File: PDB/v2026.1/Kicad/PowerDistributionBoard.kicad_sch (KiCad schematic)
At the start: 74 parts, among them J1 12V_EXP3, J10 BMS, J11 IMD, J12 Suspension_Linear_Pot1, J13 Suspension_Linear_Pot2, J14 Suspension_Linear_Pot3, J15 Suspension_Linear_Pot4, J16 CCM_Faults, J17 EXP1_5V, J18 RasPI_5V, J19 LATCH_12V, J2 12V_EXP2, J20 Throttle_Sensor, J21 Current_Sensor, J24 Wheel_Sensor1, J25 Wheel_Sensor2, J26 3V3_EXP, J27 BATTERY_12V, J28 BATTERY_GND, J29 BATTERY_24V, J3 12V_EXP1, J31 FAN1_24V, J32 FAN2_24V, J33 PUMP1_24V, J34 PUMP2_24V, J35 24V_EXP1, J4 RTM, J5 CCM_12V, J7 BSPD, J8 LATCH, J9 TSSI, U1 5to3.3_Linear_Regulator, U2 TLV76150DCYR

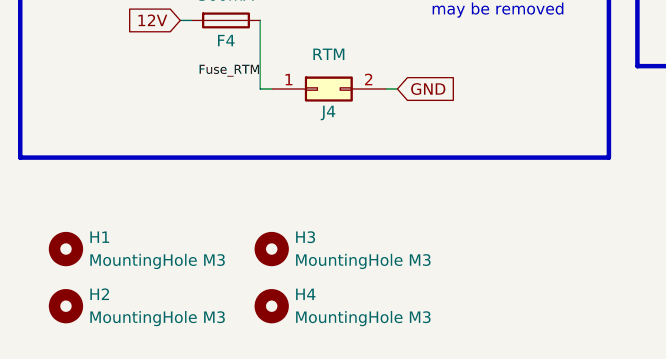
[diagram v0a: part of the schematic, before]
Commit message: Added plated mounting holes, fixed diode
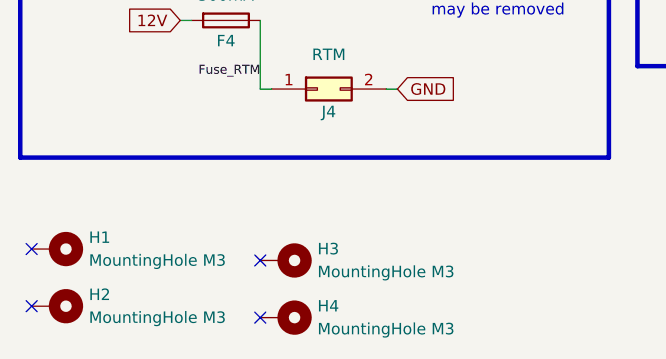
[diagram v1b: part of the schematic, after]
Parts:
- removed H1, H2, H3, H4: MountingHole M3, MountingHole:MountingHole_3.2mm_M3, symbol Mechanical:MountingHole
- added H1, H2, H3, H4: MountingHole M3, MountingHole:MountingHole_3.2mm_M3_Pad, symbol Mechanical:MountingHole_Pad
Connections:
- no-connect marks 12 -> 16

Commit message: Made quick changes: updated fuse footprint
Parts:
- F1, F10, F11, F12, F13, F14, F15, F17, F18, F19, F2, F20, F21, F24, F25, F26, F27, F29, F3, F31, F32, F33, F34, F35, F4, F5, F7, F9, FU1, FU2: footprint 0footprints:649-SERIES-HOLDER -> 0footprints:FUSE_3522-2
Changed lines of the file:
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@@
 			)
 		)
-		(property "Footprint" "0footprints:649-SERIES-HOLDER"
+		(property "Footprint" "0footprints:FUSE_3522-2"
 			(at 223.52 116.332 90)
 			(effects
@@
 			)
 		)
-		(property "Footprint" "0footprints:649-SERIES-HOLDER"
+		(property "Footprint" "0footprints:FUSE_3522-2"
 			(at 38.1 89.662 90)
 			(effects
@@
 			)
 		)
-		(property "Footprint" "0footprints:649-SERIES-HOLDER"
+		(property "Footprint" "0footprints:FUSE_3522-2"
 			(at 168.91 146.812 90)
 			(effects
@@
 			)
 		)
-		(property "Footprint" "0footprints:649-SERIES-HOLDER"
+		(property "Footprint" "0footprints:FUSE_3522-2"
 			(at 168.91 129.032 90)
 			(effects
@@
 			)
 		)
-		(property "Footprint" "0footprints:649-SERIES-HOLDER"
+		(property "Footprint" "0footprints:FUSE_3522-2"
 			(at 222.25 71.882 90)
 			(effects
@@
 			)
 		)
-		(property "Footprint" "0footprints:649-SERIES-HOLDER"
+		(property "Footprint" "0footprints:FUSE_3522-2"
 			(at 38.1 137.922 90)
 			(effects
@@
 			)
 		)
-		(property "Footprint" "0footprints:649-SERIES-HOLDER"
+		(property "Footprint" "0footprints:FUSE_3522-2"
 			(at 100.33 138.938 90)
 			(effects
@@
 			)
 		)
-		(property "Footprint" "0footprints:649-SERIES-HOLDER"
+		(property "Footprint" "0footprints:FUSE_3522-2"
 			(at 38.1 104.902 90)
 			(effects
@@
 			)
 		)
-		(property "Footprint" "0footprints:649-SERIES-HOLDER"
+		(property "Footprint" "0footprints:FUSE_3522-2"
 			(at 154.94 72.898 90)
 			(effects
@@
 			)
 		)
-		(property "Footprint" "0footprints:649-SERIES-HOLDER"
+		(property "Footprint" "0footprints:FUSE_3522-2"
 			(at 223.52 99.822 90)
 			(effects
@@
 			)
 		)
-		(property "Footprint" "0footprints:649-SERIES-HOLDER"
+		(property "Footprint" "0footprints:FUSE_3522-2"
 			(at 154.94 46.228 90)
 			(effects
@@
 			)
 		)
-		(property "Footprint" "0footprints:649-SERIES-HOLDER"
+		(property "Footprint" "0footprints:FUSE_3522-2"
 			(at 168.91 118.872 90)
 			(effects
@@
 			)
 		)
-		(property "Footprint" "0footprints:649-SERIES-HOLDER"
+		(property "Footprint" "0footprints:FUSE_3522-2"
 			(at 27.94 24.892 90)
 			(effects
@@
 			)
 		)
-		(property "Footprint" "0footprints:649-SERIES-HOLDER"
+		(property "Footprint" "0footprints:FUSE_3522-2"
 			(at 223.52 22.098 90)
 			(effects
@@
 			)
 		)
-		(property "Footprint" "0footprints:649-SERIES-HOLDER"
+		(property "Footprint" "0footprints:FUSE_3522-2"
 			(at 168.91 137.922 90)
 			(effects
@@
 			)
 		)
-		(property "Footprint" "0footprints:649-SERIES-HOLDER"
+		(property "Footprint" "0footprints:FUSE_3522-2"
 			(at 38.1 154.432 90)
 			(effects
@@
 			)
 		)
-		(property "Footprint" "0footprints:649-SERIES-HOLDER"
+		(property "Footprint" "0footprints:FUSE_3522-2"
 			(at 96.52 46.228 90)
 			(effects
@@
 			)
 		)
-		(property "Footprint" "0footprints:649-SERIES-HOLDER"
+		(property "Footprint" "0footprints:FUSE_3522-2"
 			(at 222.25 85.852 90)
 			(effects
@@
 			)
 		)
-		(property "Footprint" "0footprints:649-SERIES-HOLDER"
+		(property "Footprint" "0footprints:FUSE_3522-2"
 			(at 120.65 22.098 90)
 			(effects
@@
 			)
 		)
-		(property "Footprint" "0footprints:649-SERIES-HOLDER"
+		(property "Footprint" "0footprints:FUSE_3522-2"
 			(at 38.1 121.412 90)
 			(effects
@@
 			)
 		)
-		(property "Footprint" "0footprints:649-SERIES-HOLDER"
+		(property "Footprint" "0footprints:FUSE_3522-2"
 			(at 96.52 61.468 90)
 			(effects
@@
 			)
 		)
-		(property "Footprint" "0footprints:649-SERIES-HOLDER"
+		(property "Footprint" "0footprints:FUSE_3522-2"
 			(at 100.33 151.638 90)
 			(effects
@@
 			)
 		)
-		(property "Footprint" "0footprints:649-SERIES-HOLDER"
+		(property "Footprint" "0footprints:FUSE_3522-2"
 			(at 168.91 109.982 90)
 			(effects
@@
 			)
 		)
-		(property "Footprint" "0footprints:649-SERIES-HOLDER"
+		(property "Footprint" "0footprints:FUSE_3522-2"
 			(at 100.33 109.728 90)
 			(effects
@@
 			)
 		)
-		(property "Footprint" "0footprints:649-SERIES-HOLDER"
+		(property "Footprint" "0footprints:FUSE_3522-2"
 			(at 260.35 105.918 90)
 			(effects
@@
 			)
 		)
-		(property "Footprint" "0footprints:649-SERIES-HOLDER"
+		(property "Footprint" "0footprints:FUSE_3522-2"
 			(at 261.62 88.138 90)
 			(effects
@@
 			)
 		)
-		(property "Footprint" "0footprints:649-SERIES-HOLDER"
+		(property "Footprint" "0footprints:FUSE_3522-2"
 			(at 100.33 121.412 90)
 			(effects
@@
 			)
 		)
-		(property "Footprint" "0footprints:649-SERIES-HOLDER"
+		(property "Footprint" "0footprints:FUSE_3522-2"
 			(at 27.94 61.468 90)
 			(effects
@@
 			)
 		)
-		(property "Footprint" "0footprints:649-SERIES-HOLDER"
+		(property "Footprint" "0footprints:FUSE_3522-2"
 			(at 154.94 60.198 90)
 			(effects
@@
 			)
 		)
-		(property "Footprint" "0footprints:649-SERIES-HOLDER"
+		(property "Footprint" "0footprints:FUSE_3522-2"
 			(at 154.94 85.598 90)
 			(effects

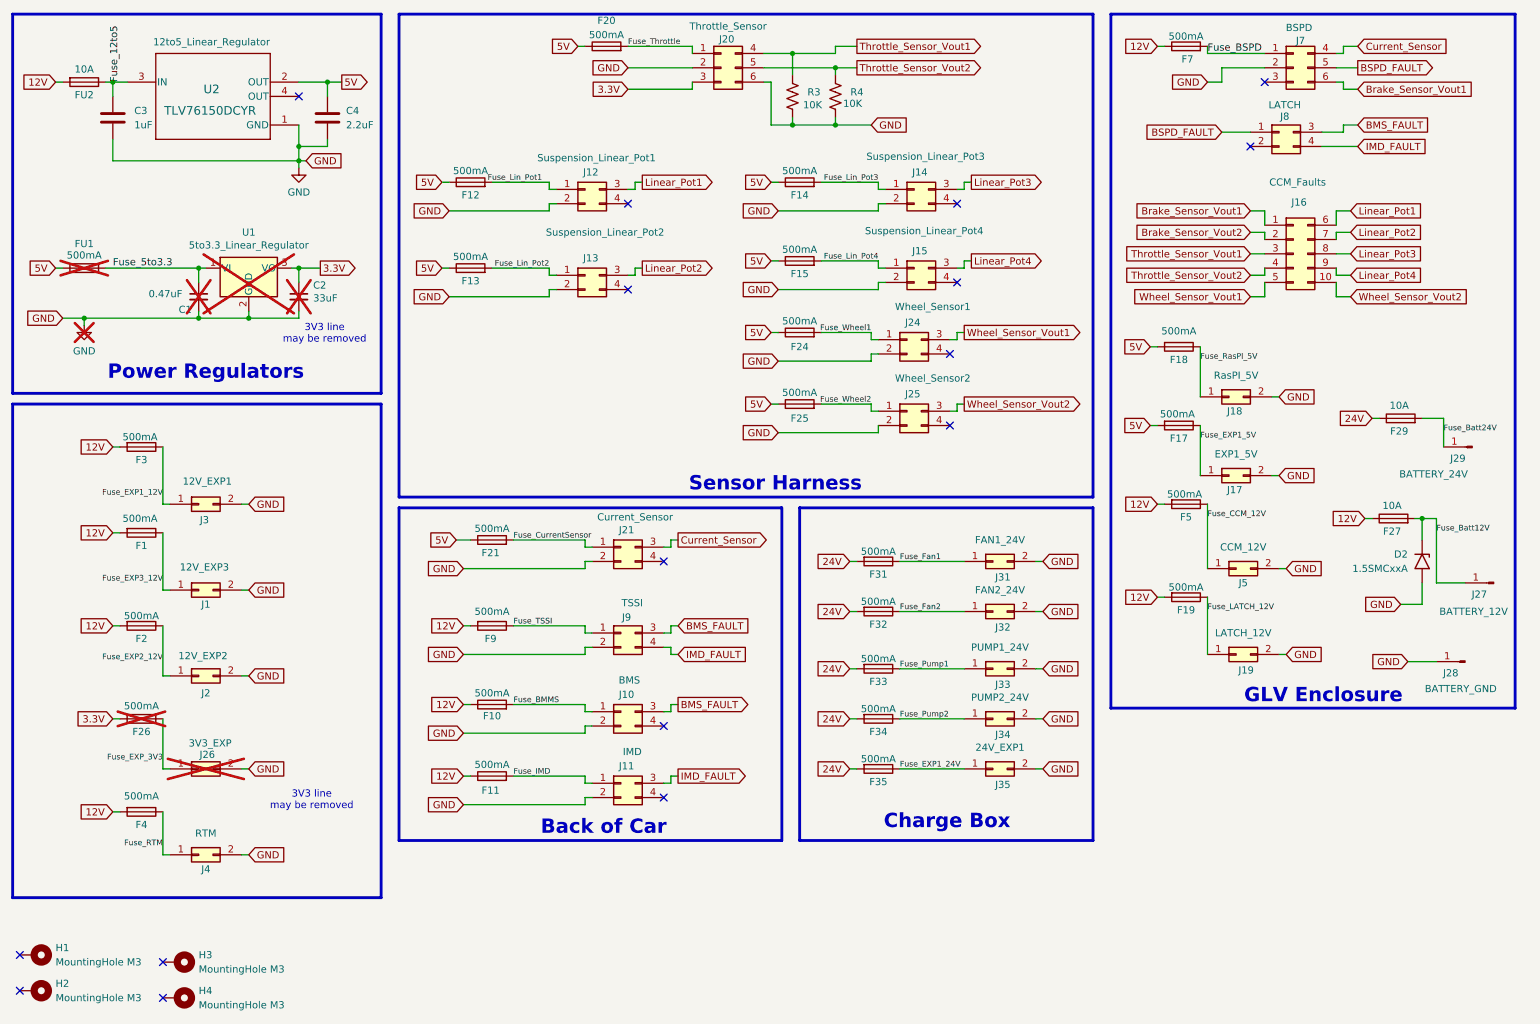
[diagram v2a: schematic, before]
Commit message: PDB: Removed most 5V fuses, made board size smaller
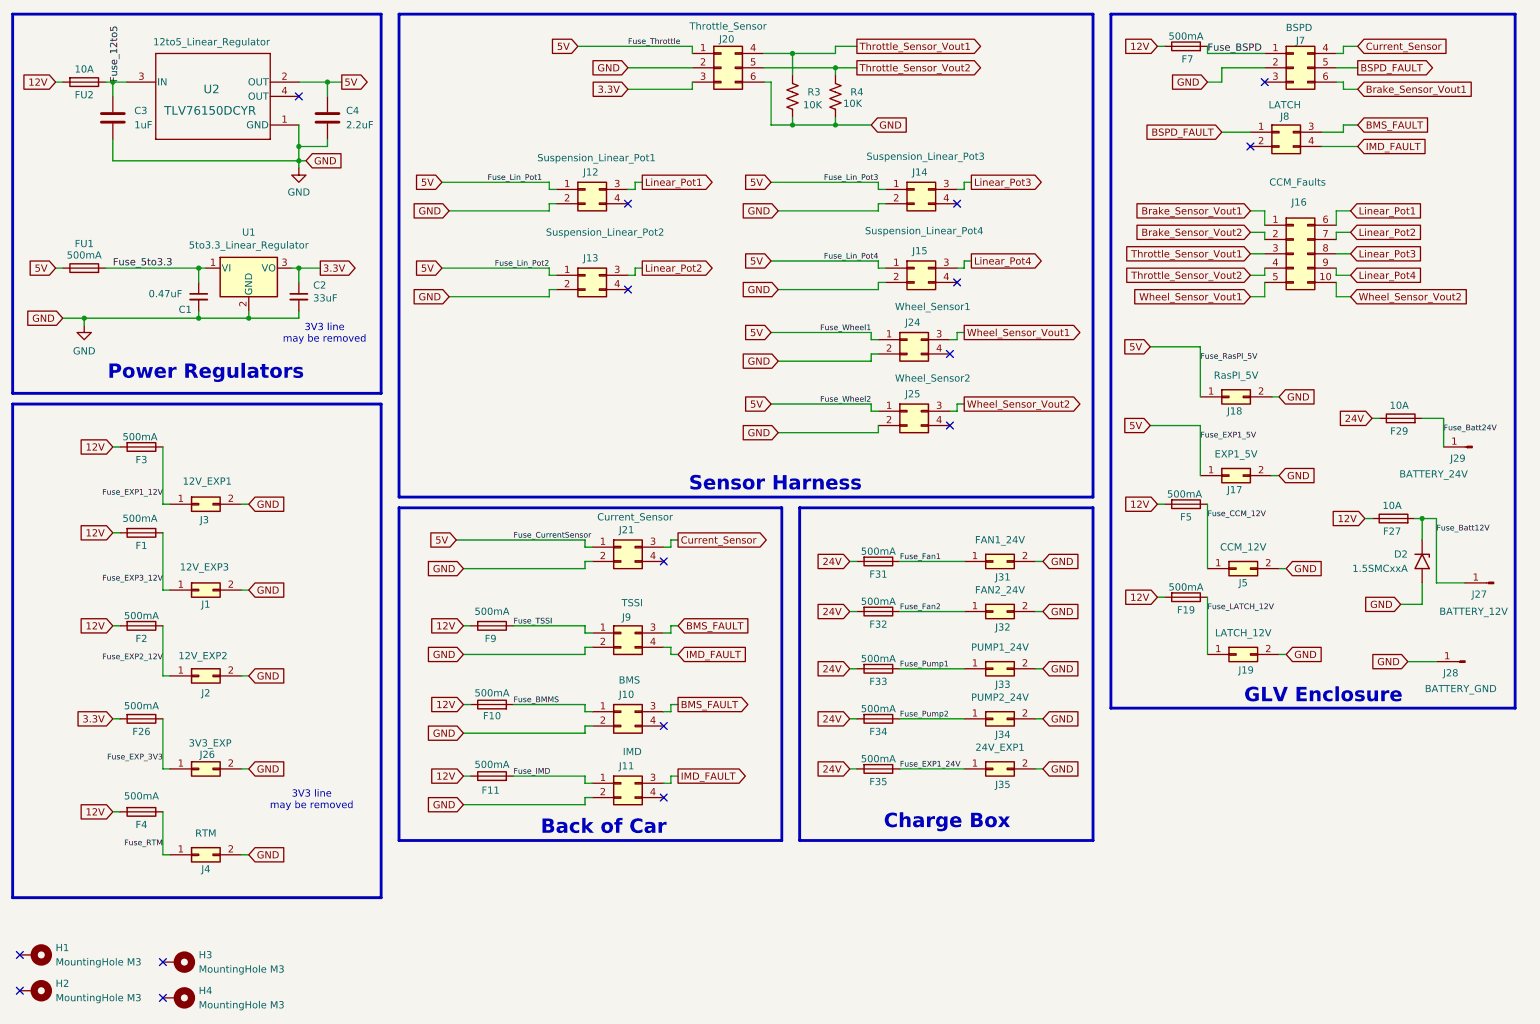
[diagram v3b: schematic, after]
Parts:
- removed F12, F13, F14, F15, F17, F18, F20, F21, F24, F25: 500mA, 0footprints:FUSE_3522-2, symbol Device:Fuse
- C1, C2, F26, FU1, J26, U1: now fitted
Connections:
- net Fuse_CurrentSensor is gone; now on net 5V: J21.1 (Pin_1)
- net Fuse_EXP1_5V is gone; now on net 5V: J17.1 (Pin_1)
- net Fuse_Lin_Pot1 is gone; now on net 5V: J12.1 (Pin_1)
- net Fuse_Lin_Pot2 is gone; now on net 5V: J13.1 (Pin_1)
- net Fuse_Lin_Pot3 is gone; now on net 5V: J14.1 (Pin_1)
- net Fuse_Lin_Pot4 is gone; now on net 5V: J15.1 (Pin_1)
- net Fuse_RasPI_5V is gone; now on net 5V: J18.1 (Pin_1)
- net Fuse_Throttle is gone; now on net 5V: J20.1 (Pin_1)
- net Fuse_Wheel1 is gone; now on net 5V: J24.1 (Pin_1)
- net Fuse_Wheel2 is gone; now on net 5V: J25.1 (Pin_1)

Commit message: Major changes for PDB schematic
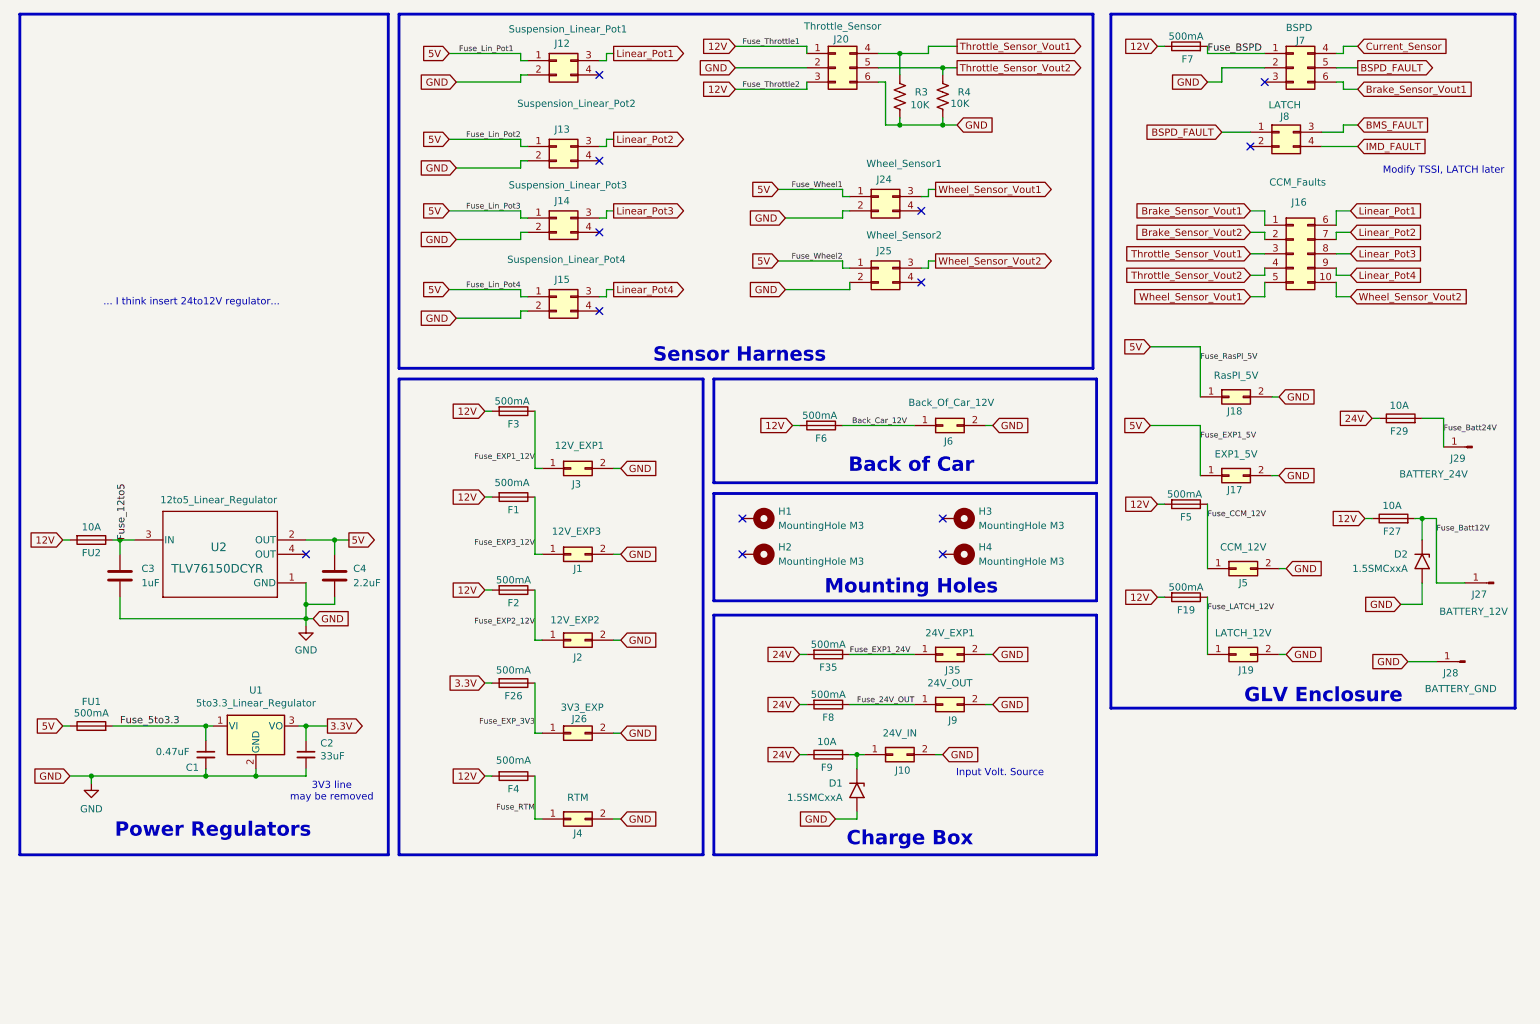
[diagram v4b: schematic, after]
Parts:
- removed F10, F11, F31, F32, F33, F34: 500mA, 0footprints:FUSE_3522-2, symbol Device:Fuse
- removed J10: BMS, 0footprints:Molex_Mini-Fit_Jr_5566-04A_2x02_P4.20mm_Vertical, symbol Connector_Generic:Conn_02x02_Top_Bottom
- removed J11: IMD, 0footprints:Molex_Mini-Fit_Jr_5566-04A_2x02_P4.20mm_Vertical, symbol Connector_Generic:Conn_02x02_Top_Bottom
- removed J21: Current_Sensor, 0footprints:Molex_Mini-Fit_Jr_5566-04A_2x02_P4.20mm_Vertical, symbol Connector_Generic:Conn_02x02_Top_Bottom
- removed J31: FAN1_24V, 0footprints:Molex_Mini-Fit_Jr_5566-02A_2x01_P4.20mm_Vertical, symbol Connector_Generic:Conn_02x01
- removed J32: FAN2_24V, 0footprints:Molex_Mini-Fit_Jr_5566-02A_2x01_P4.20mm_Vertical, symbol Connector_Generic:Conn_02x01
- removed J33: PUMP1_24V, 0footprints:Molex_Mini-Fit_Jr_5566-02A_2x01_P4.20mm_Vertical, symbol Connector_Generic:Conn_02x01
- removed J34: PUMP2_24V, 0footprints:Molex_Mini-Fit_Jr_5566-02A_2x01_P4.20mm_Vertical, symbol Connector_Generic:Conn_02x01
- removed J9: TSSI, 0footprints:Molex_Mini-Fit_Jr_5566-04A_2x02_P4.20mm_Vertical, symbol Connector_Generic:Conn_02x02_Top_Bottom
- added D1: 1.5SMCxxA, Diode_SMD:D_SMC, symbol Diode:1.5SMCxxA
- added F6, F8: 500mA, 0footprints:FUSE_3522-2, symbol Device:Fuse
- added J10: 24V_IN, 0footprints:Molex_Mini-Fit_Jr_5566-02A_2x01_P4.20mm_Vertical, symbol Connector_Generic:Conn_02x01
- added J6: Back_Of_Car_12V, 0footprints:Molex_Mini-Fit_Jr_5566-02A_2x01_P4.20mm_Vertical, symbol Connector_Generic:Conn_02x01
- added J9: 24V_OUT, 0footprints:Molex_Mini-Fit_Jr_5566-02A_2x01_P4.20mm_Vertical, symbol Connector_Generic:Conn_02x01
- F9: value 500mA -> 10A
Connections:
- net Fuse_TSSI is gone; now on net 24V: F9.1
- net 12V: now also J20.1 (Pin_1), J20.3 (Pin_3), F6.2; no longer F9.2
- net 24V: now also F8.2
- net 3.3V: no longer J20.3 (Pin_3)
- net 5V: no longer J20.1 (Pin_1)
- net GND: now also D1.2 (A2), J10.2 (Pin_2), J6.2 (Pin_2), J9.2 (Pin_2)
- new net: D1.1 (A1), F9.2, J10.1 (Pin_1)
- new net Back_Car_12V: F6.1, J6.1 (Pin_1)
- new net Fuse_24V_OUT: F8.1, J9.1 (Pin_1)
- no-connect marks 16 -> 13
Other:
- note added: "... I think insert 24to12V regulator..."
- note added: "Input Volt. Source"
- note added: "Modify TSSI, LATCH later"
- note added: "Mounting Holes"
- moved on the sheet: C1, C2, C3, C4, F1, F2, F26, F3, F35, F4, FU1, FU2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
